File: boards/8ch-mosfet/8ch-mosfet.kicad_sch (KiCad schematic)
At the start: 7 parts, among them U1 ESP32-DEVKITC

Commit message: 8 channel mosfet driver also ready for proto
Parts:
- H1, H2, H3, H4, H5: now fitted
- U1: symbol gnarboard:ESP32_DevKit_C -> yarrboard:ESP32_DevKit_C
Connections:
- net GNDD: now also H1.1, H2.1, H3.1, H4.1, H5.1
- no-connect marks 19 -> 13

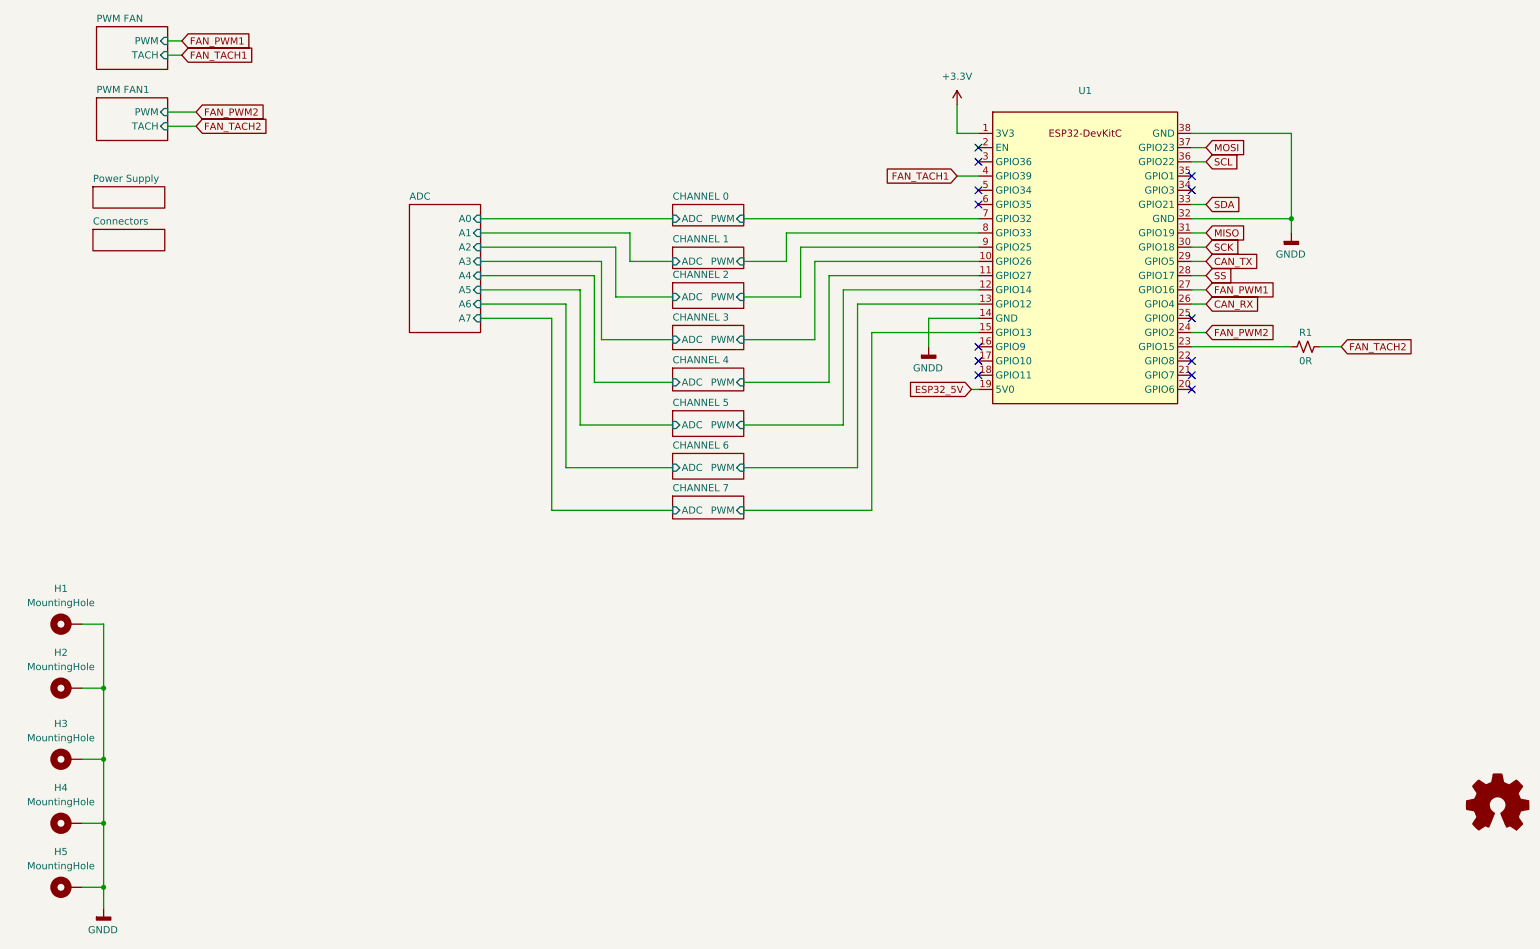
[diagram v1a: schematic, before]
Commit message: first commit of the 'totem pole' driver design
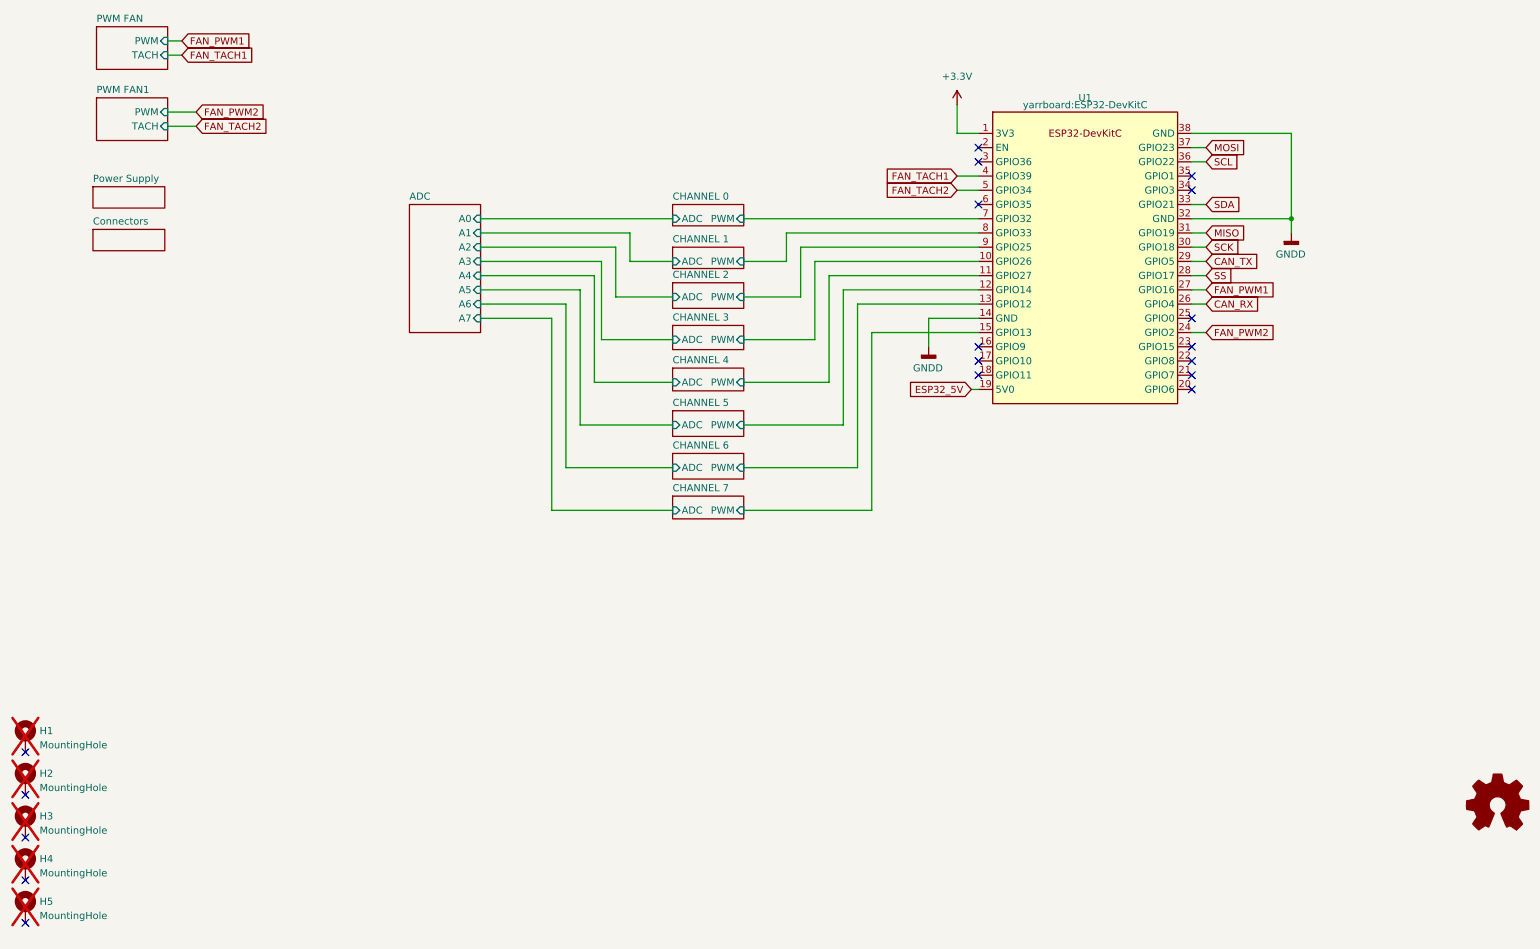
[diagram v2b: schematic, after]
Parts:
- removed R1: 0R, Resistor_SMD:R_0805_2012Metric_Pad1.20x1.40mm_HandSolder, symbol Device:R_Small_US
- H1, H2, H3, H4, H5: now not fitted
- U1: symbol yarrboard:ESP32_DevKit_C -> gnarboard:ESP32_DevKit_C
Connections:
- net FAN_TACH2: now also U1.5 (GPIO34)
- net GNDD: no longer H1.1, H2.1, H3.1, H4.1, H5.1
- no-connect marks 13 -> 18

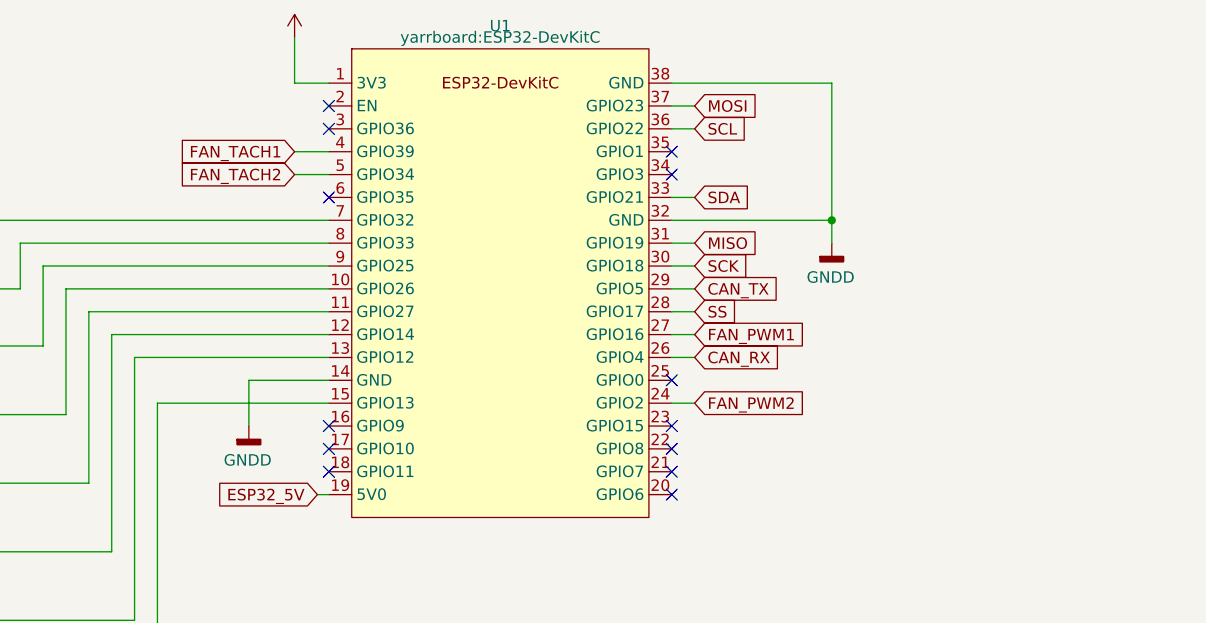
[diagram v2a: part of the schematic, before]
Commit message: updated mosfet driver schematic with changes
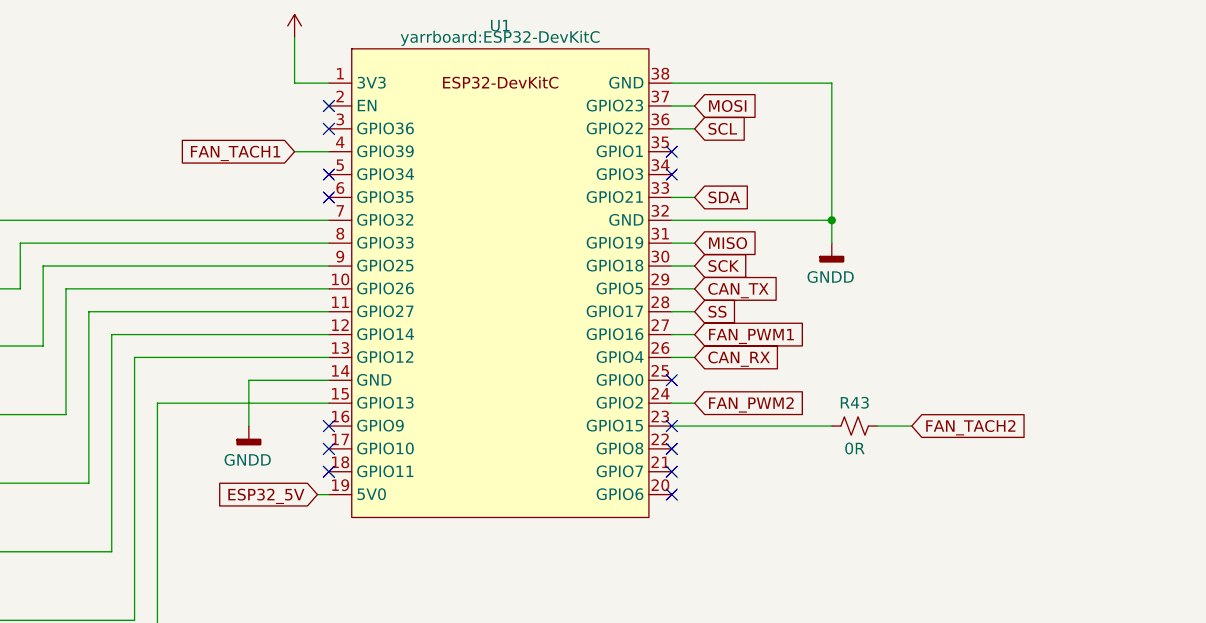
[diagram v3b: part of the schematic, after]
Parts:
- added R43: 0R, Resistor_SMD:R_0805_2012Metric_Pad1.20x1.40mm_HandSolder, symbol Device:R_Small_US
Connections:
- net FAN_TACH2: now also R43.1; no longer U1.5 (GPIO34)
- net at U1.23 (GPIO15): now also R43.2
- no-connect marks 18 -> 19
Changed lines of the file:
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@@
   (no_connect (at 185.42 92.71))
   (no_connect (at 185.42 59.69))
+  (no_connect (at 185.42 64.77))
   (no_connect (at 223.52 64.77))
   (no_connect (at 15.24 180.34))
@@
     (stroke (width 0) (type default))
   )
+  (wire (pts (xy 246.38 92.71) (xy 250.19 92.71))
+    (stroke (width 0) (type default))
+  )
   (wire (pts (xy 96.52 85.09) (xy 111.76 85.09))
     (stroke (width 0) (type default))
@@
     (stroke (width 0) (type default))
   )
+  (wire (pts (xy 223.52 92.71) (xy 241.3 92.71))
+    (stroke (width 0) (type default))
+  )
   (wire (pts (xy 241.3 72.39) (xy 241.3 69.85))
     (stroke (width 0) (type default))
@@
   )
   (wire (pts (xy 96.52 69.85) (xy 130.81 69.85))
-    (stroke (width 0) (type default))
-  )
-  (wire (pts (xy 181.61 64.77) (xy 185.42 64.77))
     (stroke (width 0) (type default))
   )
@@
     )
   )
-  (global_label "FAN_TACH2" (shape input) (at 181.61 64.77 180) (fields_autoplaced)
-    (effects (font (size 1.27 1.27)) (justify right))
-    (property "Intersheetrefs" "${INTERSHEET_REFS}" (at 168.2833 64.77 0)
-      (effects (font (size 1.27 1.27)) (justify right) hide)
+  (global_label "FAN_TACH2" (shape input) (at 250.19 92.71 0) (fields_autoplaced)
+    (effects (font (size 1.27 1.27)) (justify left))
+    (property "Intersheetrefs" "${INTERSHEET_REFS}" (at 263.5167 92.71 0)
+      (effects (font (size 1.27 1.27)) (justify left) hide)
     )
   )
@@
         )
       )
+    )
+  )
+  (symbol (lib_id "Device:R_Small_US") (at 243.84 92.71 270) (unit 1)
+    (in_bom yes) (on_board yes) (dnp no)
+    (property "Reference" "R43" (at 243.84 90.17 90)
+      (effects (font (size 1.27 1.27)))
+    )
+    (property "Value" "0R" (at 243.84 95.25 90)
+      (effects (font (size 1.27 1.27)))
+    )
+    (property "Footprint" "Resistor_SMD:R_0805_2012Metric_Pad1.20x1.40mm_HandSolder" (at 243.84 92.71 0)
+      (effects (font (size 1.27 1.27)) hide)
+    )
+    (property "Datasheet" "~" (at 243.84 92.71 0)
+      (effects (font (size 1.27 1.27)) hide)
+    )
+    (pin "1")
+    (pin "2")
+    (instances
+      (project "8ch-mosfet"
+        (path "/c83c6236-96e9-46ad-9d7a-9e2efa4a7966"
+          (reference "R43") (unit 1)
+        )
+        (path "/c83c6236-96e9-46ad-9d7a-9e2efa4a7966/0eec6767-666b-42c0-ba36-2a83c9caeade"
+          (reference "R1") (unit 1)
+        )
+        (path "/c83c6236-96e9-46ad-9d7a-9e2efa4a7966/ccdb1c25-8d0f-4f30-ab70-bbc1ecf3f6f7"
+          (reference "R5") (unit 1)
+        )
+        (path "/c83c6236-96e9-46ad-9d7a-9e2efa4a7966/1e692482-a022-407a-8cb5-d9a3b23521a6"
+          (reference "R9") (unit 1)
+        )
+        (path "/c83c6236-96e9-46ad-9d7a-9e2efa4a7966/5952e660-2bb6-45cf-b9ea-f7a7c2d0954e"
+          (reference "R13") (unit 1)
+        )
+        (path "/c83c6236-96e9-46ad-9d7a-9e2efa4a7966/772d44f5-8758-48db-a140-72ed8e75e88c"
+          (reference "R17") (unit 1)
+        )
+        (path "/c83c6236-96e9-46ad-9d7a-9e2efa4a7966/424e7b24-5644-46f2-85bb-1e459a343705"
+          (reference "R21") (unit 1)
+        )
+        (path "/c83c6236-96e9-46ad-9d7a-9e2efa4a7966/4c1df725-56ca-4be4-8107-a39054acbca4"
+          (reference "R25") (unit 1)
+        )
+        (path "/c83c6236-96e9-46ad-9d7a-9e2efa4a7966/a8a81147-5613-4820-beb3-a7ca76d0db8e"
+          (reference "R29") (unit 1)
+        )
+        (path "/c83c6236-96e9-46ad-9d7a-9e2efa4a7966/e112a34f-fd2f-43cb-bf5d-a7f5e57b6bef"
+          (reference "R37") (unit 1)
+        )
+      )

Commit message: worked on the pwm issues
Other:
- added sheet Untitled Sheet (untitled.kicad_sch)
- added sheet Untitled Sheet2 (untitled2.kicad_sch)
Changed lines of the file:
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@@
+    )
+  )
+  (sheet (at 77.47 160.02) (size 40.64 5.08) (fields_autoplaced)
+    (stroke (width 0.1524) (type solid))
+    (fill (color 0 0 0 0.0000))
+    (property "Sheetname" "Untitled Sheet2" (at 77.47 159.3084 0)
+      (effects (font (size 1.27 1.27)) (justify left bottom))
+    )
+    (property "Sheetfile" "untitled2.kicad_sch" (at 77.47 165.6846 0)
+      (effects (font (size 1.27 1.27)) (justify left top))
+    )
+    (instances
+      (project "8ch-mosfet"
+        (path "/c83c6236-96e9-46ad-9d7a-9e2efa4a7966" (page "16"))
+      )
+    )
+  )
+  (sheet (at 74.93 144.78) (size 43.18 8.89) (fields_autoplaced)
+    (stroke (width 0.1524) (type solid))
+    (fill (color 0 0 0 0.0000))
+    (property "Sheetname" "Untitled Sheet" (at 74.93 144.0684 0)
+      (effects (font (size 1.27 1.27)) (justify left bottom))
+    )
+    (property "Sheetfile" "untitled.kicad_sch" (at 74.93 154.2546 0)
+      (effects (font (size 1.27 1.27)) (justify left top))
+    )
+    (instances
+      (project "8ch-mosfet"
+        (path "/c83c6236-96e9-46ad-9d7a-9e2efa4a7966" (page "15"))
+      )
     )
   )

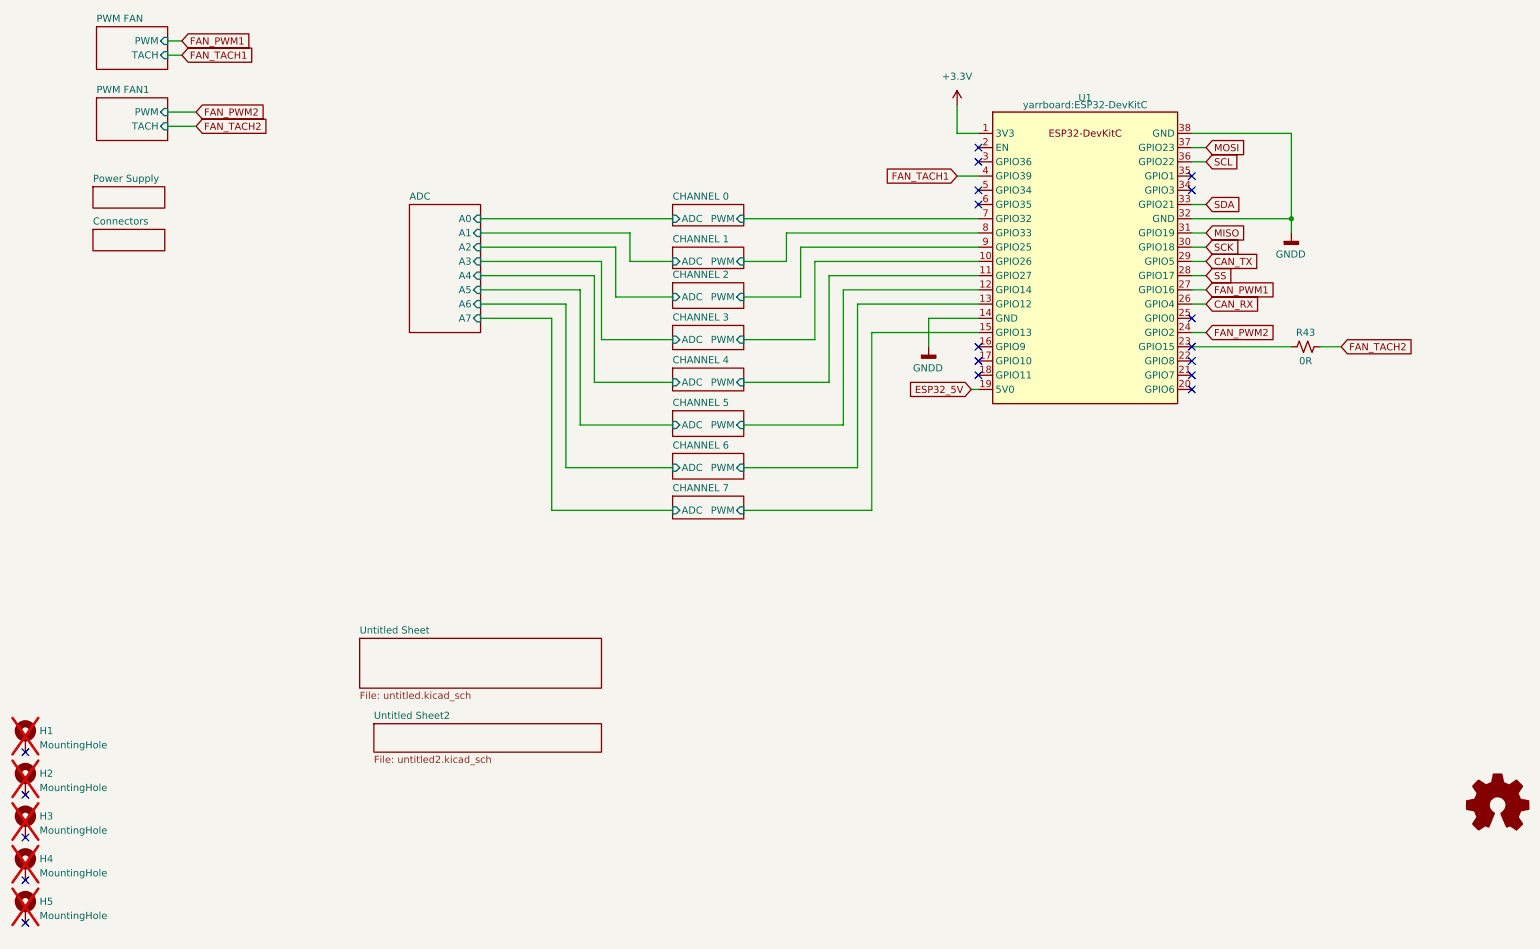
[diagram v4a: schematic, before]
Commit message: starting a redesign ahead of having parts to test. wish me luck
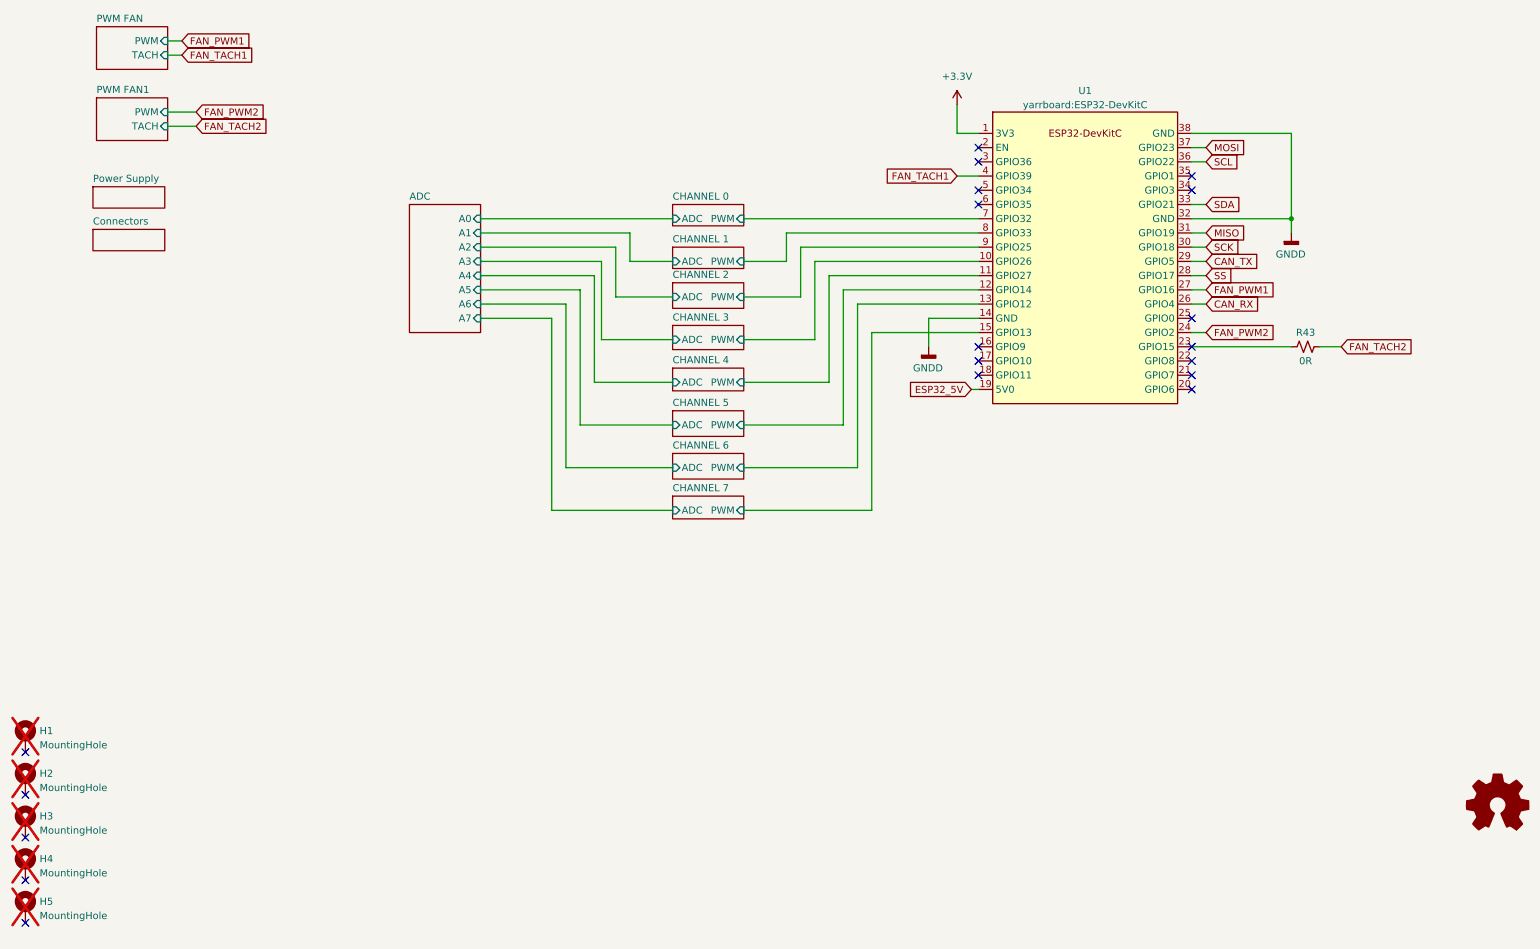
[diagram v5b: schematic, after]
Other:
- removed sheet Untitled Sheet
- removed sheet Untitled Sheet2
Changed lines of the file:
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@@
   (symbol (lib_id "gnarboard:ESP32_DevKit_C") (at 204.47 76.2 0) (unit 1)
     (in_bom yes) (on_board yes) (dnp no)
-    (property "Reference" "U1" (at 204.47 48.26 0)
+    (property "Reference" "U1" (at 204.47 46.99 0)
       (effects (font (size 1.27 1.27)))
     )
@@
       )
     )
-  )
-  (sheet (at 77.47 160.02) (size 40.64 5.08) (fields_autoplaced)
-    (stroke (width 0.1524) (type solid))
-    (fill (color 0 0 0 0.0000))
-    (property "Sheetname" "Untitled Sheet2" (at 77.47 159.3084 0)
-      (effects (font (size 1.27 1.27)) (justify left bottom))
-    )
-    (property "Sheetfile" "untitled2.kicad_sch" (at 77.47 165.6846 0)
-      (effects (font (size 1.27 1.27)) (justify left top))
-    )
-    (instances
-      (project "8ch-mosfet"
-        (path "/c83c6236-96e9-46ad-9d7a-9e2efa4a7966" (page "16"))
-      )
-    )
-  )
-  (sheet (at 74.93 144.78) (size 43.18 8.89) (fields_autoplaced)
-    (stroke (width 0.1524) (type solid))
-    (fill (color 0 0 0 0.0000))
-    (property "Sheetname" "Untitled Sheet" (at 74.93 144.0684 0)
-      (effects (font (size 1.27 1.27)) (justify left bottom))
-    )
-    (property "Sheetfile" "untitled.kicad_sch" (at 74.93 154.2546 0)
-      (effects (font (size 1.27 1.27)) (justify left top))
-    )
-    (instances
-      (project "8ch-mosfet"
-        (path "/c83c6236-96e9-46ad-9d7a-9e2efa4a7966" (page "15"))
-      )
-    )
